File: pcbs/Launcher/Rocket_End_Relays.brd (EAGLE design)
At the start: 40 parts, among them IC2 LM2576T-ADJ, K4 LD105, K5 LD105, K6 LD105, K7 LD105, T1 BC547, T2 BC547, T3 BC547, T4 BC547, T5 BC547, U1 ARDUINO-MEGAPRO-5V, X1 1751248, X2 22-23-2041, X3 22-23-2021, X4 1751248, X5 22-23-2021

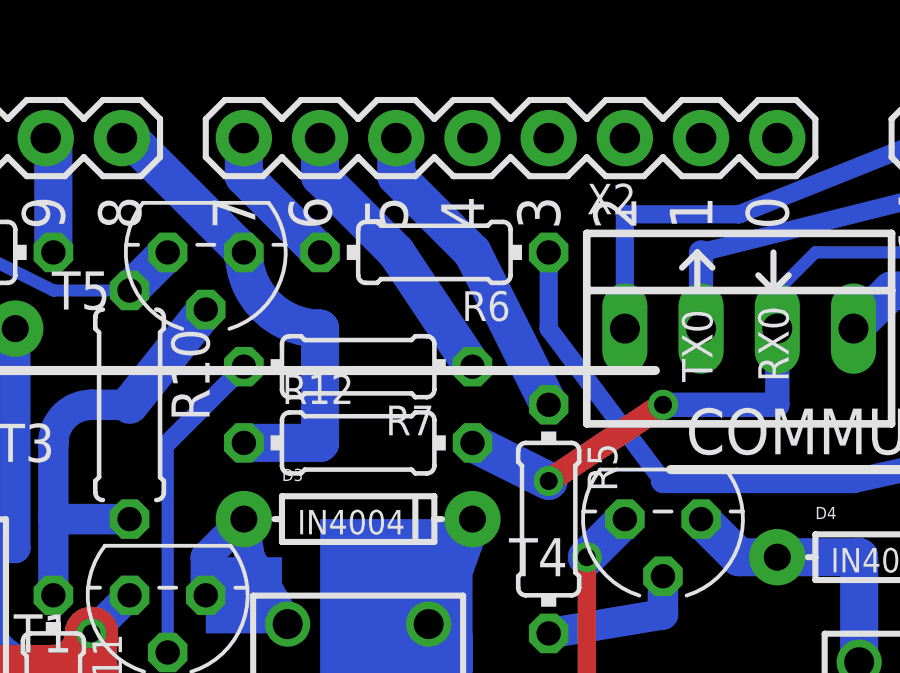
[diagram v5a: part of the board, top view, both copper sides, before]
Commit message: * Re-route launch pin to pin 3 instead and keep all other pins as they were.
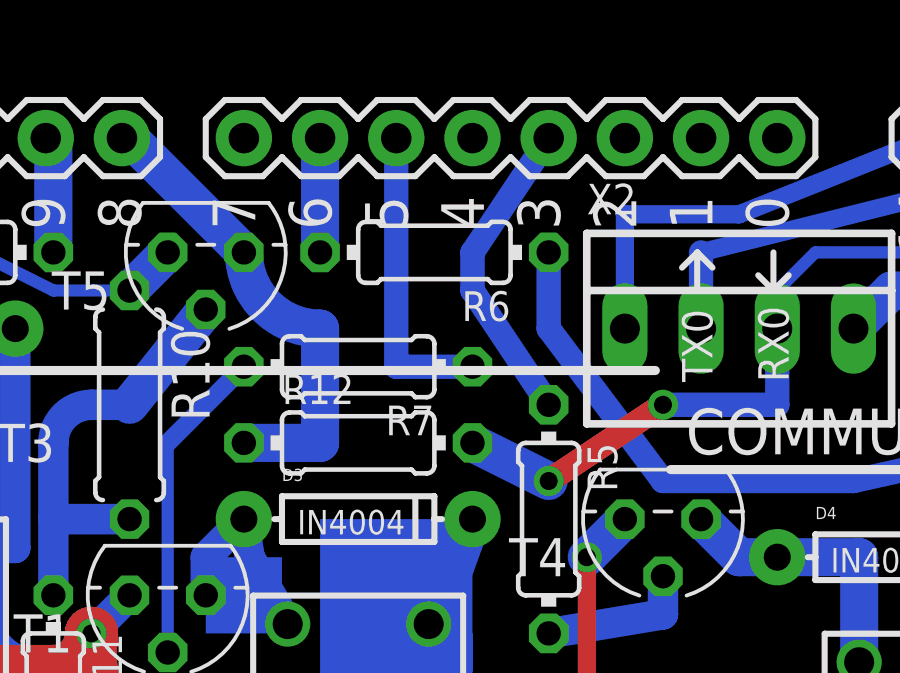
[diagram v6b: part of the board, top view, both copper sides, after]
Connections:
- net N$4: now also R7.1; no longer R5.1
- net N$8: now also R5.1, U1.3; no longer R7.1, U1.6
- net N$9: now also U1.6; no longer U1.7
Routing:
- net N$9: track 4.86 -> 3.81 mm
- net N$8: track 9.44 -> 10.4 mm
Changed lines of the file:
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@@
 <wire x1="50.8" y1="12.7" x2="50.8" y2="10.16" width="1.27" layer="16"/>
-</signal>
-<signal name="N$4">
-<contactref element="R5" pad="1"/>
-<wire x1="45.72" y1="54.61" x2="48.26" y2="49.53" width="1.27" layer="16"/>
-<contactref element="U1" pad="5"/>
-<wire x1="43.18" y1="58.42" x2="43.18" y2="57.15" width="1.27" layer="16"/>
-<wire x1="43.18" y1="57.15" x2="45.72" y2="54.61" width="1.27" layer="16"/>
 </signal>
 <signal name="N$9">
 <contactref element="R6" pad="2"/>
-<contactref element="U1" pad="7"/>
-<wire x1="40.64" y1="54.61" x2="38.1" y2="57.15" width="1.27" layer="16"/>
-<wire x1="38.1" y1="57.15" x2="38.1" y2="58.42" width="1.27" layer="16"/>
+<wire x1="40.64" y1="54.61" x2="40.64" y2="58.42" width="1.27" layer="16"/>
+<contactref element="U1" pad="6"/>
 </signal>
 <signal name="N$10">
 <contactref element="R6" pad="1"/>
 <contactref element="T2" pad="2"/>
-<wire x1="48.26" y1="54.61" x2="48.26" y2="52.07" width="0.6096" layer="16"/>
-<wire x1="48.26" y1="52.07" x2="52.07" y2="46.99" width="0.6096" layer="16"/>
+<wire x1="48.26" y1="54.61" x2="48.26" y2="52.07" width="0.8128" layer="16"/>
+<wire x1="48.26" y1="52.07" x2="52.07" y2="46.99" width="0.8128" layer="16"/>
 <wire x1="52.07" y1="46.99" x2="58.42" y2="46.99" width="0.8128" layer="16"/>
 <wire x1="64.135" y1="48.26" x2="58.42" y2="46.99" width="0.8128" layer="16"/>
@@
 <wire x1="8.89" y1="52.07" x2="8.89" y2="49.53" width="1.9304" layer="16"/>
 </signal>
+<signal name="N$4">
+<contactref element="R7" pad="1"/>
+<contactref element="U1" pad="5"/>
+<wire x1="45.72" y1="50.8" x2="43.18" y2="50.8" width="0.8128" layer="16"/>
+<wire x1="43.18" y1="50.8" x2="43.18" y2="58.42" width="0.8128" layer="16"/>
+</signal>
 <signal name="N$8">
-<contactref element="R7" pad="1"/>
-<contactref element="U1" pad="6"/>
-<wire x1="45.72" y1="50.8" x2="43.18" y2="54.61" width="1.27" layer="16"/>
-<wire x1="43.18" y1="54.61" x2="40.64" y2="57.15" width="1.27" layer="16"/>
-<wire x1="40.64" y1="57.15" x2="40.64" y2="58.42" width="1.27" layer="16"/>
+<contactref element="R5" pad="1"/>
+<contactref element="U1" pad="3"/>
+<wire x1="48.26" y1="58.42" x2="45.72" y2="54.61" width="0.8128" layer="16"/>
+<wire x1="45.72" y1="54.61" x2="45.72" y2="53.34" width="0.8128" layer="16"/>
+<wire x1="45.72" y1="53.34" x2="48.26" y2="49.53" width="0.8128" layer="16"/>
 </signal>
 </signals>

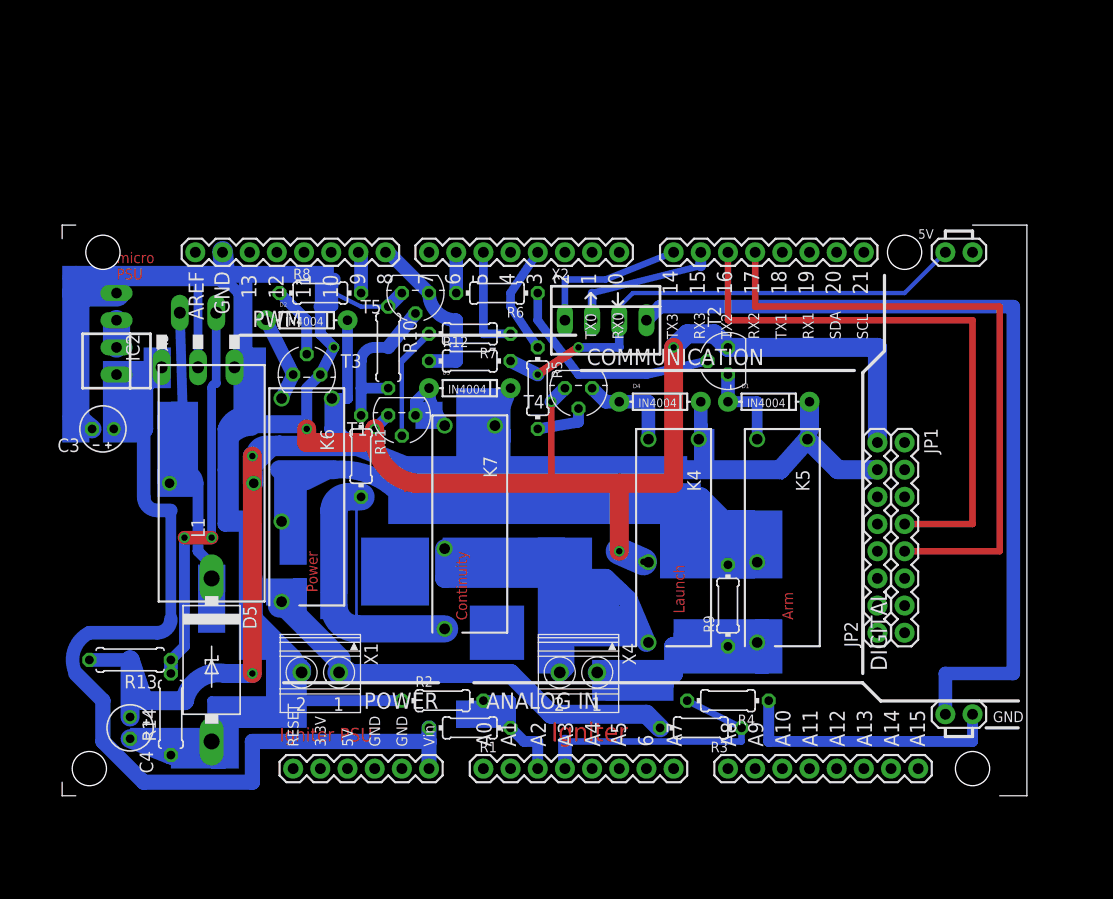
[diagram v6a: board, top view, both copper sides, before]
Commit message: * Lots of adjustments to track to deal with issues that EaglePCB finds.
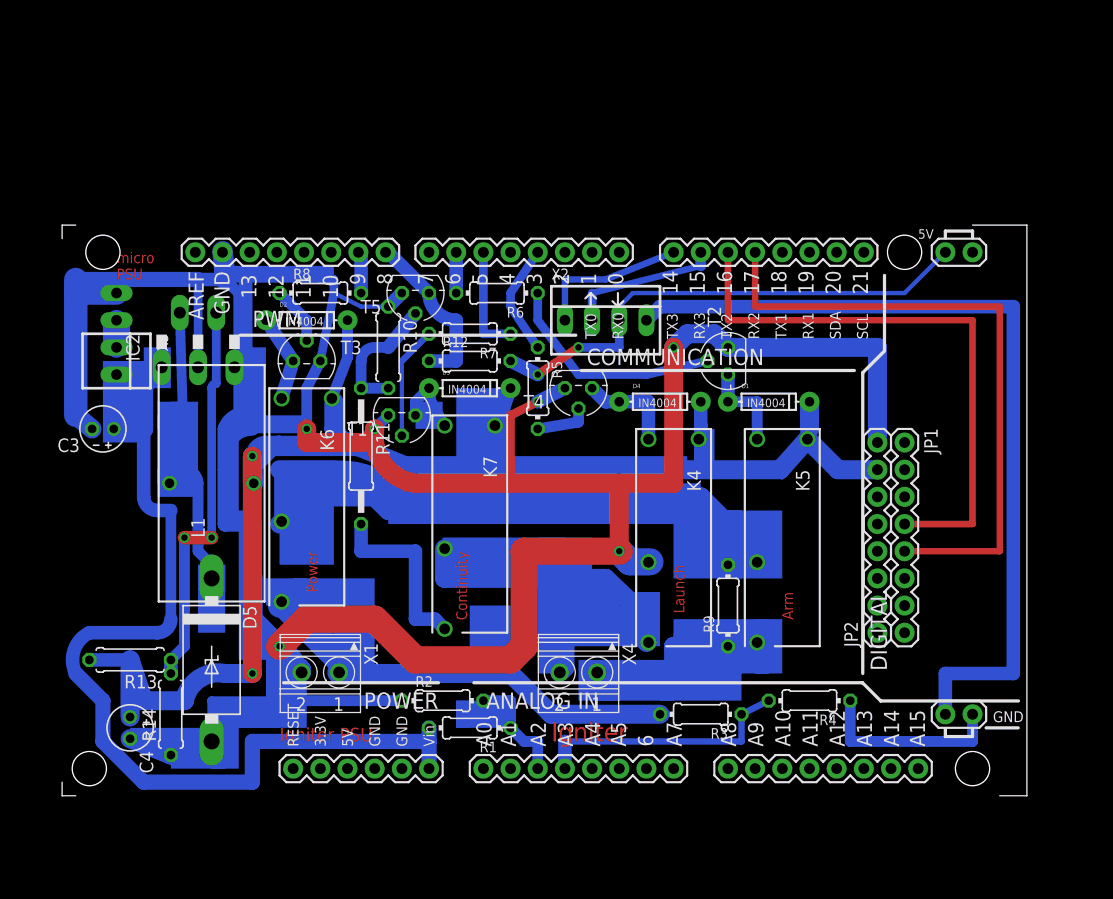
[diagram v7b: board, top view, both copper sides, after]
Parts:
- R11: device rcl:0204/7 -> resistor:0207/12
- moved R4 7.62 mm to (73.7, 16.5)
- moved R3 1.27 mm to (63.5, 15.2)
- moved T3 1.27 mm to (26.7, 48.3)
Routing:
- net N$33: track 275.0 -> 313.6 mm, vias 7 -> 6
- net N$30: track 36.8 -> 17.1 mm
- net N$28: track 68.5 -> 81.5 mm
- net N$24: track 25.4 -> 17.8 mm
- net N$31: track 14.8 -> 12.2 mm
- net N$3: track 26.0 -> 24.4 mm
- net N$11: track 6.77 -> 5.50 mm
- net N$5: track 162.4 -> 161.2 mm
- net N$29: track 41.5 -> 40.9 mm

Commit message: * More refinements to tracks.
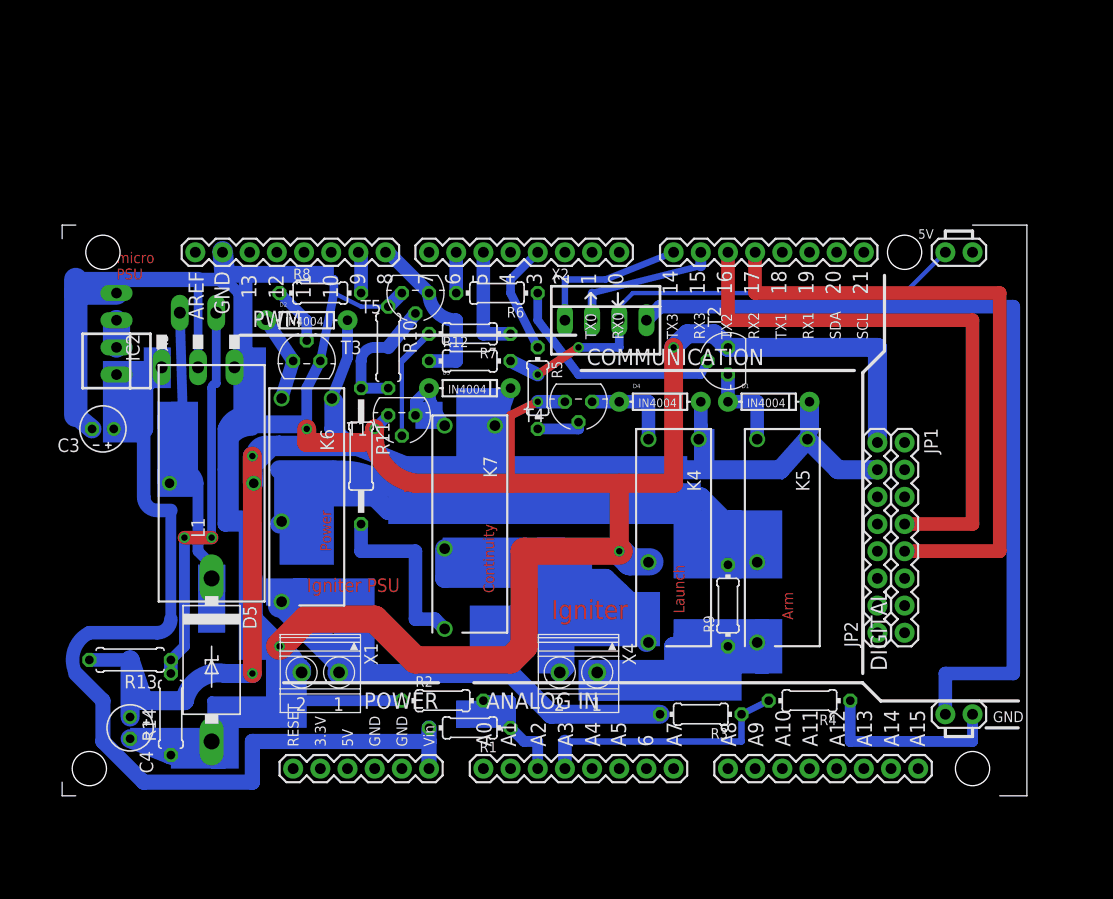
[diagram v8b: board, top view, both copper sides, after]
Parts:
- moved T4 1.27 mm to (52.1, 44.5)
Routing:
- net N$12: track 5.13 -> 4.45 mm
- net N$10: track 21.1 -> 21.7 mm
- net N$19: track 9.30 -> 8.77 mm
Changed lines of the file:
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@@
 <board>
 <plain>
-<text x="26.67" y="30.48" size="1.016" layer="1" rot="R270">Power</text>
+<text x="27.94" y="34.29" size="1.016" layer="1" rot="R270">Power</text>
 <text x="71.12" y="26.67" size="1.016" layer="1" rot="R270">Arm</text>
 <text x="60.96" y="29.21" size="1.016" layer="1" rot="R270">Launch</text>
-<text x="40.64" y="30.48" size="1.016" layer="1" rot="R270">Continuity</text>
-<text x="24.13" y="12.7" size="1.27" layer="1">Igniter PSU</text>
+<text x="43.18" y="33.02" size="1.016" layer="1" rot="R270">Continuity</text>
+<text x="26.67" y="26.67" size="1.27" layer="1">Igniter PSU</text>
 <text x="8.89" y="55.88" size="1.016" layer="1">micro
 PSU</text>
@@
 <rectangle x1="17.78" y1="10.16" x2="19.05" y2="15.24" layer="16"/>
 <rectangle x1="17.78" y1="10.16" x2="20.32" y2="15.24" layer="16"/>
-<text x="49.53" y="12.7" size="1.778" layer="1">Igniter</text>
+<text x="49.53" y="24.13" size="1.778" layer="1">Igniter</text>
 <rectangle x1="21.59" y1="41.91" x2="26.67" y2="43.18" layer="16"/>
 <rectangle x1="22.86" y1="39.37" x2="31.75" y2="40.64" layer="16"/>
@@
 <element name="T2" library="transistor-neu-to92" package="TO92" value="BC547" x="66.04" y="48.26" rot="R90"/>
 <element name="T3" library="transistor-neu-to92" package="TO92" value="BC547" x="26.67" y="48.26"/>
-<element name="T4" library="transistor-neu-to92" package="TO92" value="BC547" x="52.07" y="45.72" rot="R180"/>
+<element name="T4" library="transistor-neu-to92" package="TO92" value="BC547" x="52.07" y="44.45" rot="R180"/>
 <element name="T5" library="transistor" package="TO92" value="BC547" x="36.83" y="54.61" rot="R180"/>
 <element name="U1" library="JoeMega_Ether_Edited" package="ARDUINO_MEGA-PRO-5V" value="ARDUINO-MEGAPRO-5V" x="3.81" y="7.62"/>
@@
 <wire x1="48.26" y1="54.61" x2="48.26" y2="52.07" width="0.8128" layer="16"/>
 <wire x1="48.26" y1="52.07" x2="52.07" y2="46.99" width="0.8128" layer="16"/>
-<wire x1="52.07" y1="46.99" x2="58.42" y2="46.99" width="0.8128" layer="16"/>
-<wire x1="64.135" y1="48.26" x2="58.42" y2="46.99" width="0.8128" layer="16"/>
+<wire x1="52.07" y1="46.99" x2="63.5" y2="46.99" width="0.8128" layer="16"/>
+<wire x1="64.135" y1="48.26" x2="63.5" y2="46.99" width="0.8128" layer="16"/>
 </signal>
 <signal name="N$11">
@@
 <contactref element="R5" pad="2"/>
 <contactref element="T4" pad="2"/>
-<wire x1="52.07" y1="43.815" x2="52.07" y2="42.545" width="1.016" layer="16"/>
-<wire x1="52.07" y1="42.545" x2="48.26" y2="41.91" width="1.016" layer="16"/>
+<wire x1="52.07" y1="42.545" x2="52.07" y2="41.91" width="1.016" layer="16"/>
+<wire x1="52.07" y1="41.91" x2="48.26" y2="41.91" width="1.016" layer="16"/>
 </signal>
 <signal name="N$13">
@@
 <wire x1="55.88" y1="44.45" x2="58.61" y2="44.45" width="1.27" layer="16"/>
 <wire x1="58.61" y1="44.45" x2="58.61" y2="40.95" width="1.27" layer="16"/>
-<wire x1="53.34" y1="45.72" x2="54.61" y2="44.45" width="1.27" layer="16"/>
-<wire x1="54.61" y1="44.45" x2="55.88" y2="44.45" width="1.27" layer="16"/>
+<wire x1="53.34" y1="44.45" x2="55.88" y2="44.45" width="1.27" layer="16"/>
 </signal>
 <signal name="N$20">
@@
 <contactref element="K5" pad="2"/>
 <contactref element="D1" pad="A"/>
-<wire x1="68.77" y1="44.45" x2="68.77" y2="40.95" width="1.016" layer="16"/>
-<wire x1="68.77" y1="44.45" x2="66.04" y2="44.45" width="1.016" layer="16"/>
+<wire x1="68.77" y1="44.45" x2="68.77" y2="40.95" width="1.27" layer="16"/>
+<wire x1="68.77" y1="44.45" x2="66.04" y2="44.45" width="1.27" layer="16"/>
 <wire x1="66.04" y1="44.45" x2="66.04" y2="46.99" width="1.27" layer="16"/>
 </signal>
@@
 <signal name="N$1">
 <contactref element="U1" pad="16"/>
-<wire x1="66.04" y1="58.42" x2="66.04" y2="52.07" width="0.6096" layer="1"/>
+<wire x1="66.04" y1="58.42" x2="66.04" y2="52.07" width="1.27" layer="1"/>
 <contactref element="JP1" pad="4"/>
-<wire x1="66.04" y1="52.07" x2="88.9" y2="52.07" width="0.6096" layer="1"/>
-<wire x1="88.9" y1="52.07" x2="88.9" y2="33.02" width="0.6096" layer="1"/>
-<wire x1="88.9" y1="33.02" x2="82.55" y2="33.02" width="0.6096" layer="1"/>
+<wire x1="66.04" y1="52.07" x2="88.9" y2="52.07" width="1.27" layer="1"/>
+<wire x1="88.9" y1="52.07" x2="88.9" y2="33.02" width="1.27" layer="1"/>
+<wire x1="88.9" y1="33.02" x2="82.55" y2="33.02" width="1.27" layer="1"/>
 </signal>
 <signal name="N$2">
 <contactref element="U1" pad="17"/>
-<wire x1="68.58" y1="58.42" x2="68.58" y2="53.34" width="0.6096" layer="1"/>
-<wire x1="68.58" y1="53.34" x2="91.44" y2="53.34" width="0.6096" layer="1"/>
-<wire x1="91.44" y1="53.34" x2="91.44" y2="30.48" width="0.6096" layer="1"/>
+<wire x1="68.58" y1="58.42" x2="68.58" y2="54.61" width="1.27" layer="1"/>
+<wire x1="68.58" y1="54.61" x2="91.44" y2="54.61" width="1.27" layer="1"/>
+<wire x1="91.44" y1="54.61" x2="91.44" y2="30.48" width="1.27" layer="1"/>
 <contactref element="JP1" pad="5"/>
-<wire x1="91.44" y1="30.48" x2="82.55" y2="30.48" width="0.6096" layer="1"/>
+<wire x1="91.44" y1="30.48" x2="82.55" y2="30.48" width="1.27" layer="1"/>
 </signal>
 <signal name="N$14">
@@
 <wire x1="16.51" y1="55.88" x2="5.08" y2="55.88" width="1.4224" layer="16"/>
 <wire x1="13.97" y1="11.43" x2="10.16" y2="12.954" width="1.778" layer="16"/>
-<wire x1="48.26" y1="44.45" x2="50.8" y2="45.72" width="1.27" layer="16"/>
+<wire x1="48.26" y1="44.45" x2="50.8" y2="44.45" width="1.27" layer="16"/>
 <wire x1="19.9136" y1="47.6692" x2="20.32" y2="48.26" width="0.6096" layer="16"/>
 <wire x1="34.29" y1="43.18" x2="33.02" y2="41.91" width="1.016" layer="16"/>
@@
 <contactref element="R7" pad="1"/>
 <contactref element="U1" pad="5"/>
-<wire x1="45.72" y1="50.8" x2="43.18" y2="50.8" width="0.8128" layer="16"/>
-<wire x1="43.18" y1="50.8" x2="43.18" y2="58.42" width="0.8128" layer="16"/>
+<wire x1="45.72" y1="50.8" x2="43.18" y2="50.8" width="1.27" layer="16"/>
+<wire x1="43.18" y1="50.8" x2="43.18" y2="58.42" width="1.27" layer="16"/>
 </signal>
 <signal name="N$8">
 <contactref element="R5" pad="1"/>
 <contactref element="U1" pad="3"/>
-<wire x1="48.26" y1="58.42" x2="45.72" y2="54.61" width="0.8128" layer="16"/>
-<wire x1="45.72" y1="54.61" x2="45.72" y2="53.34" width="0.8128" layer="16"/>
-<wire x1="45.72" y1="53.34" x2="48.26" y2="49.53" width="0.8128" layer="16"/>
+<wire x1="48.26" y1="58.42" x2="45.72" y2="55.88" width="0.8128" layer="16"/>
+<wire x1="45.72" y1="55.88" x2="45.72" y2="54.61" width="0.8128" layer="16"/>
+<wire x1="45.72" y1="54.61" x2="48.26" y2="49.53" width="0.8128" layer="16"/>
 </signal>
 <signal name="N$28">
